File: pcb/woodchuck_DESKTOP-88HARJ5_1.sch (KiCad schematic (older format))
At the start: 1 part

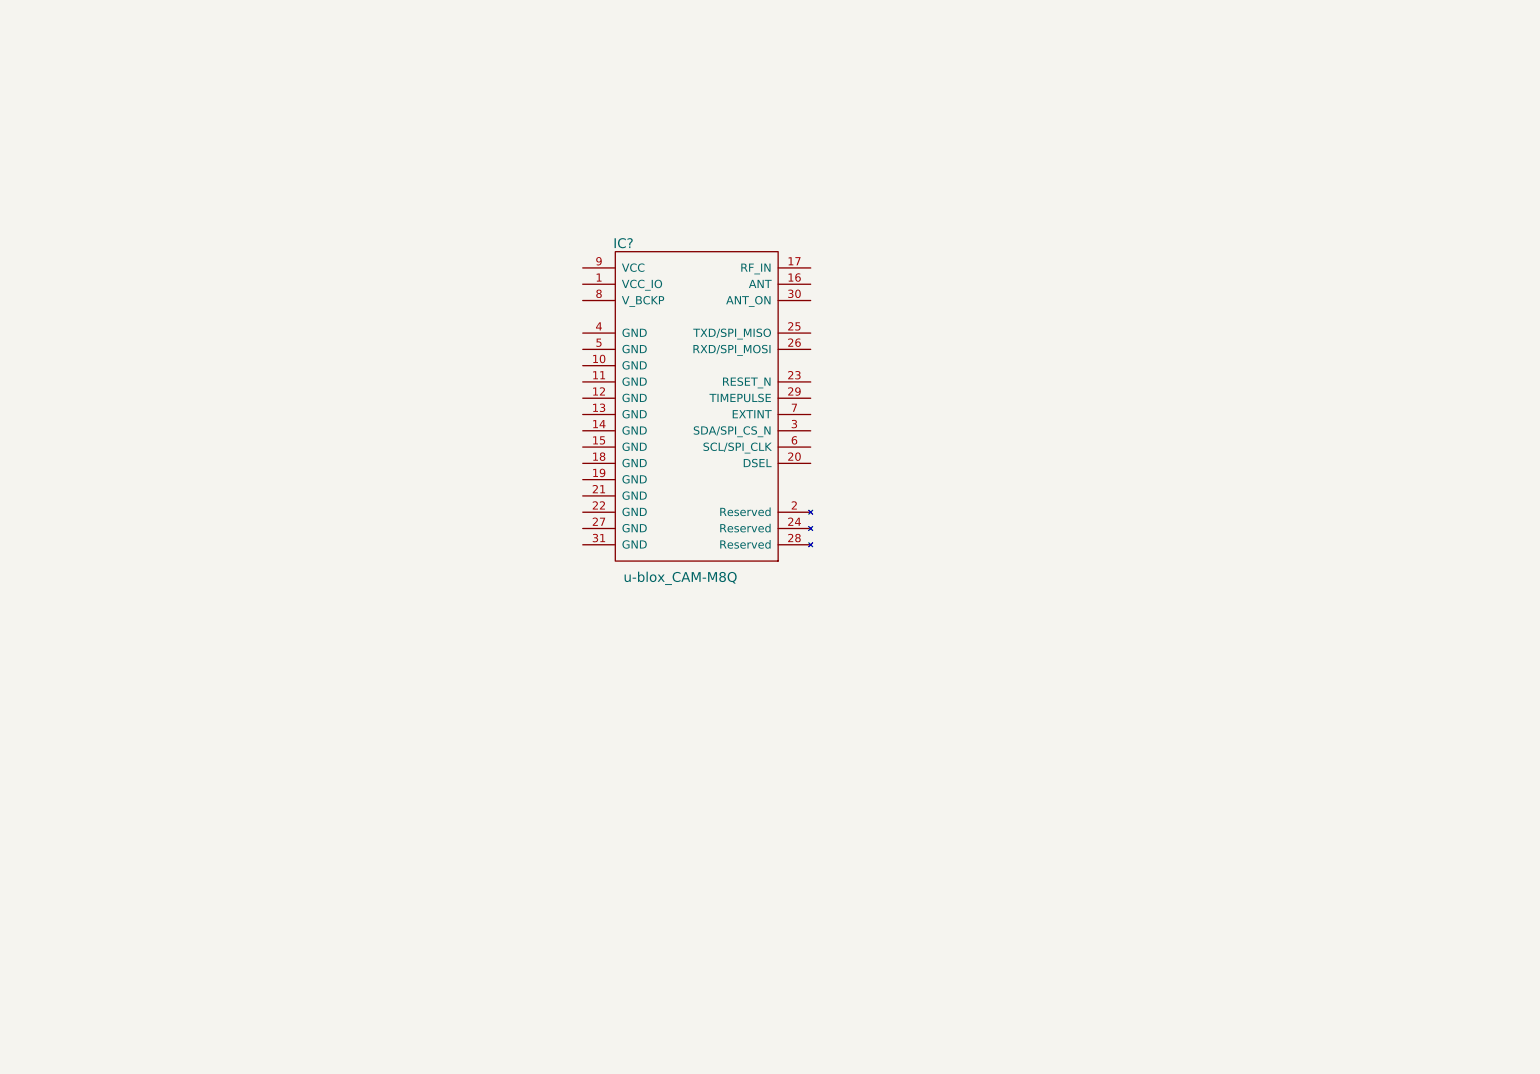
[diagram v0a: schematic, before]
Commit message: Add MTX2 circuit and add a sheet for power supply/regulation
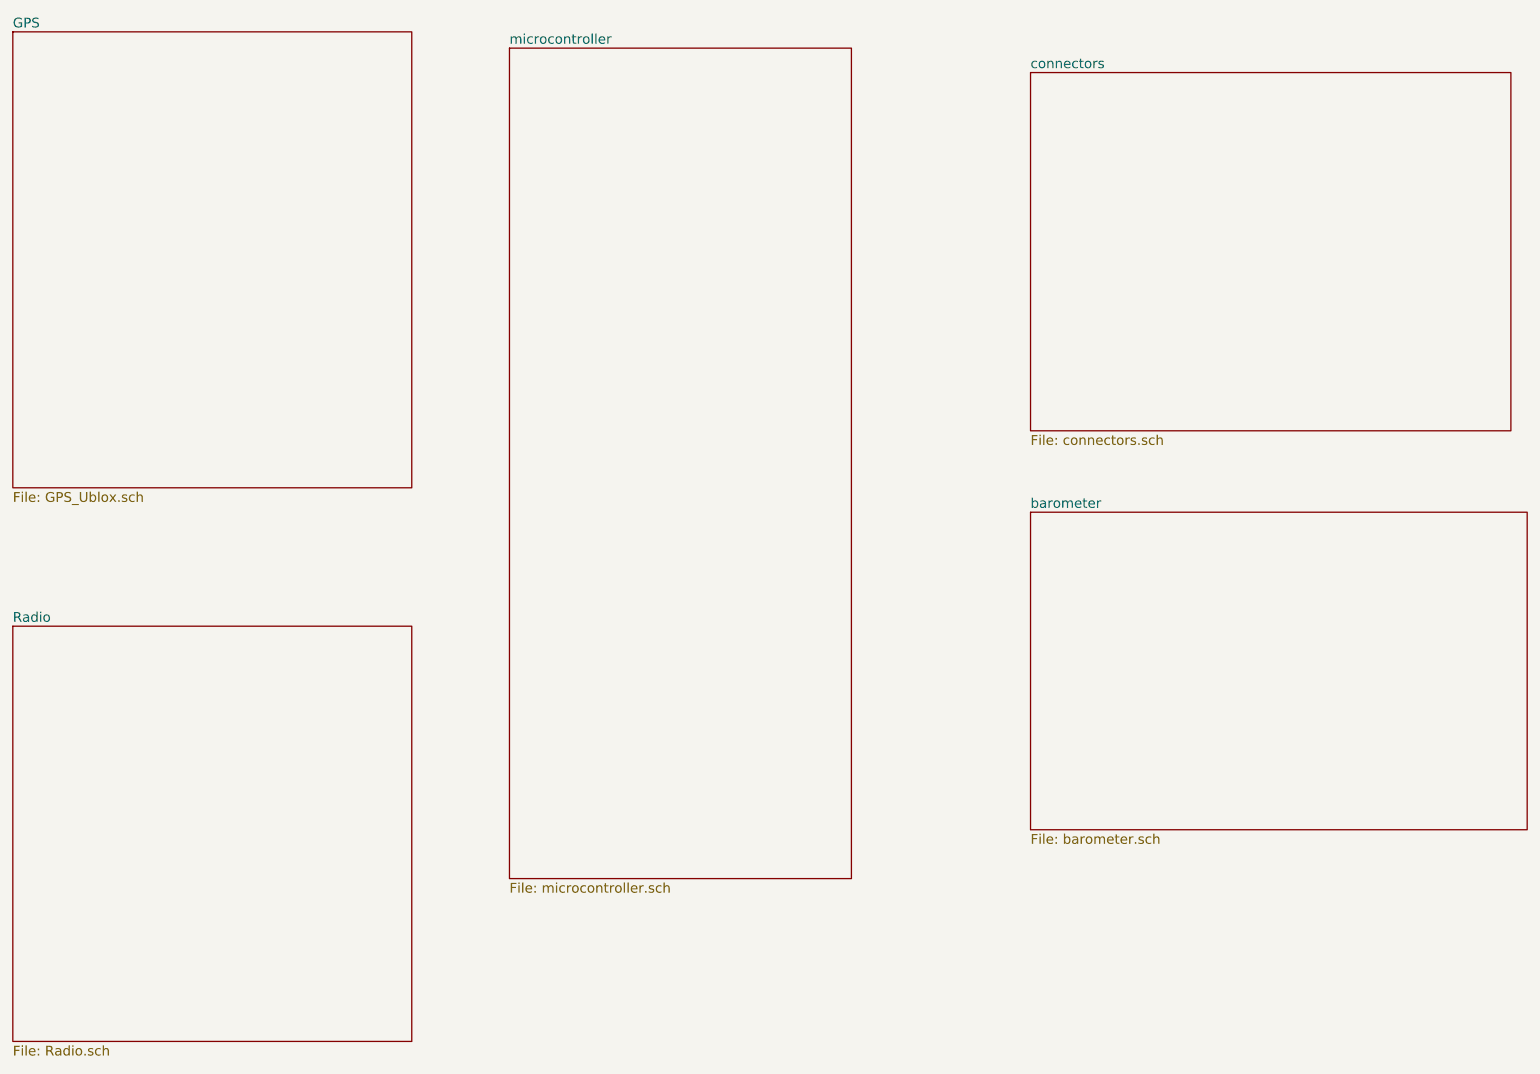
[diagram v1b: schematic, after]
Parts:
- removed IC?: u-blox_CAM-M8Q, symbol u-blox_CAM-M8Q
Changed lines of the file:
@@
 LIBS:max-7q
 LIBS:ms5611-01ba03
+LIBS:quarter_wave_ant
 LIBS:resistor
 LIBS:rfm69w
+LIBS:sma
 LIBS:stm32f405vgt
 LIBS:swd
@@
 LIBS:uSD_holder
 LIBS:radiometrix_mtx2
-LIBS:stm32f072cbt6
-LIBS:jsta
-LIBS:sma
-LIBS:cga0402mlc-12g
 LIBS:woodchuck-cache
 EELAYER 25 0
@@
 $Descr A4 11693 8268
 encoding utf-8
-Sheet 2 7
+Sheet 1 6
 Title ""
 Date ""
@@
 Comment4 ""
 $EndDescr
-$Comp
-L u-blox_CAM-M8Q IC?
-U 1 1 565D0659
-P 5350 2900
-F 0 "IC?" H 4900 3450 60  0000 C CNN
-F 1 "u-blox_CAM-M8Q" H 5250 1400 60  0000 C CNN
-F 2 "" H 5550 2000 60  0000 C CNN
-F 3 "" H 5550 2000 60  0000 C CNN
-	1    5350 2900
-	1    0    0    -1
-$EndComp
+$Sheet
+S 1150 1050 2450 2800
+U 56574088
+F0 "GPS" 60
+F1 "GPS_Ublox.sch" 60
+$EndSheet
+$Sheet
+S 1150 4700 2450 2550
+U 5657408B
+F0 "Radio" 60
+F1 "Radio.sch" 60
+$EndSheet
+$Sheet
+S 4200 1150 2100 5100
+U 56574098
+F0 "microcontroller" 60
+F1 "microcontroller.sch" 60
+$EndSheet
+$Sheet
+S 7400 1300 2950 2200
+U 5657409B
+F0 "connectors" 60
+F1 "connectors.sch" 60
+$EndSheet
+$Sheet
+S 7400 4000 3050 1950
+U 5657409E
+F0 "barometer" 60
+F1 "barometer.sch" 60
+$EndSheet
 $EndSCHEMATC
